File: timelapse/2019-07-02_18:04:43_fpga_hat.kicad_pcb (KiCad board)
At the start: 4 copper layers, 65 x 56.5 mm, 90 parts, among them J1 2x20, J2 AudioJack3, J3 Conn_02x06_Top_Bottom, J4 Conn_02x06_Top_Bottom, J5 Conn_02x06_Top_Bottom, J6 Conn_01x02, SW1 PTS815, SW2 PTS815, SW3 PTS815, SW4 PTS815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

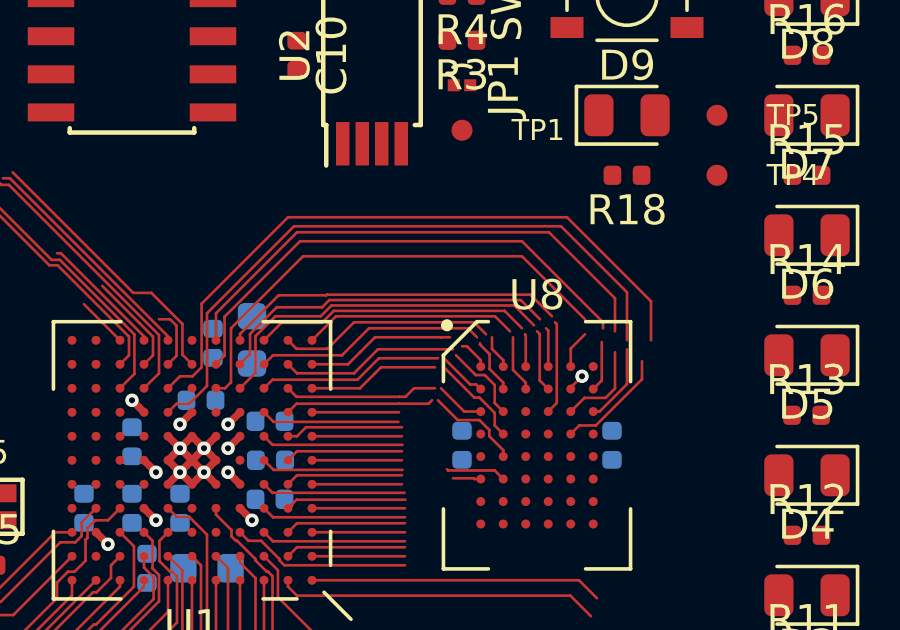
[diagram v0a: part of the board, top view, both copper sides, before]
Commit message: Continue FPGA escape. Start escaping SRAM.
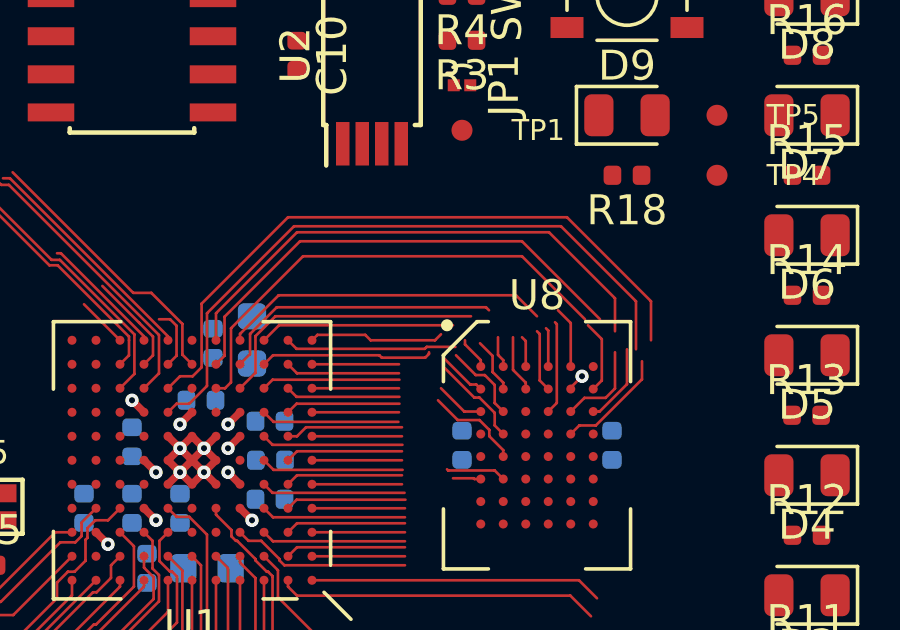
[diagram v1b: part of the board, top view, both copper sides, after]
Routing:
- net /SRAM_A15: track 9.25 -> 6.51 mm
- net /SRAM_A10: track 7.14 -> 4.53 mm
- net /SRAM_A14: track 11.9 -> 9.41 mm
- net /SRAM_A6: track 9.07 -> 6.94 mm
- net /SRAM_A5: track 4.97 -> 2.90 mm
- net /SRAM_A17: track 11.5 -> 9.52 mm
- net /SRAM_A13: track 7.72 -> 5.76 mm
- net /SRAM_A11: track 6.21 -> 4.63 mm
- net /SRAM_A12: track 7.25 -> 5.72 mm
- net /SRAM_A4: track 6.47 -> 4.98 mm
- net /SRAM_A7: track 5.14 -> 3.83 mm
- net /SRAM_A3: track 6.87 -> 5.73 mm
- net /SRAM_A2: track 4.17 -> 4.95 mm
- net /SRAM_DQ0: track 4.78 -> 5.53 mm
- net /SRAM_A16: track 11.5 -> 10.9 mm
